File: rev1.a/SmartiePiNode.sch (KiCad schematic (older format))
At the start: 48 parts, among them CN1 USBMICROb, CN2 ST-LINK, CN3 SX1238_TRX_HEADER, SW1 SW_PUSH, U1 ISL91127IR, U2 STM32L052_LQFP48, X1 8MHz(16pF), X2 ABS25-32.768KHZ-6-T

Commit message: footprints
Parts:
- C1, C10, C11, C12, C13, C14, C15, C16, C17, C18, C19, C2, C3, C4, C5, C6, C7, C8, C9: footprint (none) -> Capacitors_SMD:C_0603
- CN1: footprint (none) -> amphenol-microusb-10118194:amphenol-microusb-10118194
- CN2: footprint (none) -> Pin_Headers:Pin_Header_Straight_1x05
- CN3: footprint (none) -> Pin_Headers:Pin_Header_Straight_2x10
- D1: footprint (none) -> digikey-footprints:MicroSD_2908-05WB-MG
- R1, R10, R11, R12, R13, R14, R2, R3, R4, R5, R6, R7, R8, R9: footprint (none) -> Resistors_SMD:R_0603
- SD1: footprint MF_Connectors_MF-MICROSD -> amphenol-microsd-114-00841-68:amphenol-microsd-1140084168
- U1: footprint (none) -> Housings_DFN_QFN:QFN-20-1EP_4x4mm_Pitch0.5mm
- U2: footprint (none) -> Housings_QFP:LQFP-48_7x7mm_Pitch0.5mm

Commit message: hse selection and footprint
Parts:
- removed X2: ABS25-32.768KHZ-6-T, symbol Crystal_Small
- added X?: ABS25-32.768KHZ-6-T, symbol abracon-abs25
- BT1: footprint (none) -> mpd-bh123a:mpd-BH123A
- X1: footprint (none) -> Crystals:Crystal_HC49-SD_SMD
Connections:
- net at C19.2, R14.1: now also X?.1
- net at C18.2, R13.1: now also X?.4
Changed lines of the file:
@@
 LIBS:sw-push
 LIBS:micro-sd-card
+LIBS:crystal_small
 LIBS:SmartiePiNode-cache
 EELAYER 26 0
@@
 F 0 "X1" V 6745 2780 50  0000 L CNN
 F 1 "8MHz(16pF)" V 6960 2595 50  0000 L CNN
-F 2 "" H 6815 2740 50  0001 C CNN
+F 2 "Crystals:Crystal_HC49-SD_SMD" H 6815 2740 50  0001 C CNN
 F 3 "" H 6815 2740 50  0001 C CNN
 	1    6815 2740
@@
 Wire Wire Line
 	10140 2790 9825 2790
-$Comp
-L Crystal_Small X2
-U 1 1 5B098328
-P 10575 2835
-F 0 "X2" V 10510 2870 50  0000 L CNN
-F 1 "ABS25-32.768KHZ-6-T" V 10775 2070 50  0000 L CNN
-F 2 "" H 10575 2835 50  0001 C CNN
-F 3 "" H 10575 2835 50  0001 C CNN
-	1    10575 2835
-	0    1    1    0
-$EndComp
 Wire Wire Line
 	10340 2890 10395 2890
@@
 U 1 1 5B098883
 P 10870 2735
-F 0 "C18" V 10830 2805 50  0000 C CNN
+F 0 "C18" V 10835 2640 50  0000 C CNN
 F 1 "4.3pF" V 10965 2735 50  0000 C CNN
 F 2 "Capacitors_SMD:C_0603" H 10870 2735 50  0001 C CNN
@@
 U 1 1 5B098936
 P 10870 2935
-F 0 "C19" V 10830 3005 50  0000 C CNN
+F 0 "C19" V 10835 2840 50  0000 C CNN
 F 1 "4.3pF" V 10975 2930 50  0000 C CNN
 F 2 "Capacitors_SMD:C_0603" H 10870 2935 50  0001 C CNN
@@
 F 0 "BT1" V 1380 3135 50  0000 L CNN
 F 1 "CR123A" V 1650 3070 50  0000 L CNN
-F 2 "" V 1525 3220 50  0001 C CNN
+F 2 "mpd-bh123a:mpd-BH123A" V 1525 3220 50  0001 C CNN
 F 3 "" V 1525 3220 50  0001 C CNN
 	1    1525 3160
@@
 Text Notes 5500 5950 0    39   ~ 0
 second stage output filter goes here.
+$Comp
+L abracon-abs25 X?
+U 1 1 5B12A6FF
+P 10575 2835
+F 0 "X?" V 10510 2880 50  0000 L CNN
+F 1 "ABS25-32.768KHZ-6-T" V 10765 2080 50  0000 L CNN
+F 2 "" H 10575 2835 50  0001 C CNN
+F 3 "" H 10575 2835 50  0001 C CNN
+	1    10575 2835
+	0    1    1    0
+$EndComp
 $EndSCHEMATC

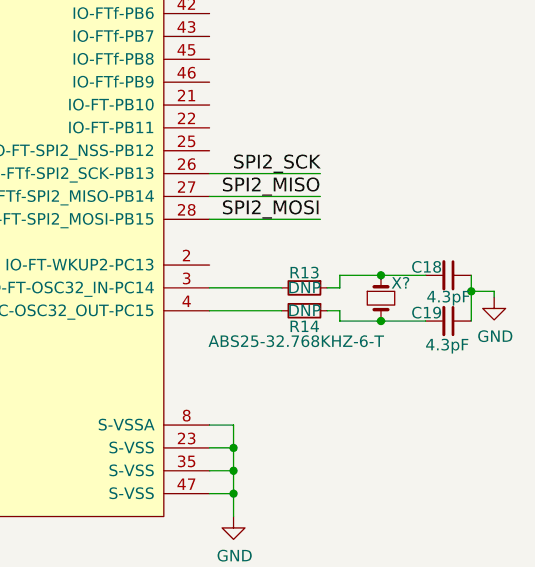
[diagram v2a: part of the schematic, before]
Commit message: L1 part selection, footprint and 3d model creation.
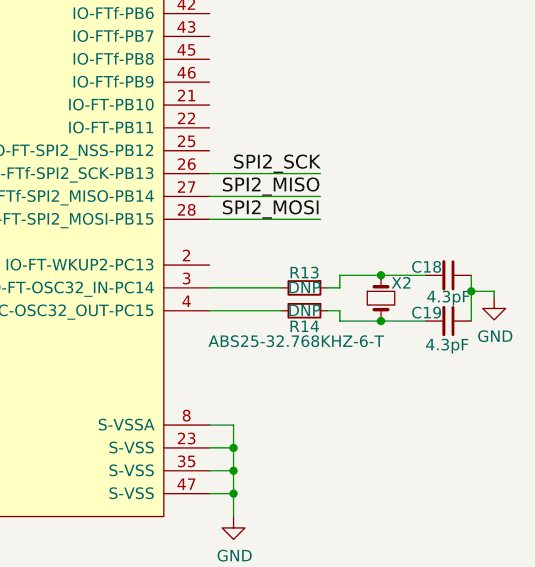
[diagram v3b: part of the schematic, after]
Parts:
- L1: footprint (none) -> murata-1277AS-H-1R0M:murata-1277AS-H-1R0M
- X2: renamed from X?; footprint (none) -> abracon-abs25:abracon-abs25
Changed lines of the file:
@@
 F 0 "L1" V 3565 5480 50  0000 C CNN
 F 1 "1uH" V 3460 5485 50  0000 C CNN
-F 2 "" H 3500 5480 50  0001 C CNN
+F 2 "murata-1277AS-H-1R0M:murata-1277AS-H-1R0M" H 3500 5480 50  0001 C CNN
 F 3 "" H 3500 5480 50  0001 C CNN
 	1    3500 5480
@@
 second stage output filter goes here.
 $Comp
-L abracon-abs25 X?
+L abracon-abs25 X2
 U 1 1 5B12A6FF
 P 10575 2835
-F 0 "X?" V 10510 2880 50  0000 L CNN
+F 0 "X2" V 10510 2880 50  0000 L CNN
 F 1 "ABS25-32.768KHZ-6-T" V 10765 2080 50  0000 L CNN
-F 2 "" H 10575 2835 50  0001 C CNN
+F 2 "abracon-abs25:abracon-abs25" H 10575 2835 50  0001 C CNN
 F 3 "" H 10575 2835 50  0001 C CNN
 	1    10575 2835

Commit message: x1 and x2 footprint and 3d models added to cvpcb
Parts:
- D1: footprint digikey-footprints:MicroSD_2908-05WB-MG -> Diodes_SMD:SOD-123
- D2: footprint (none) -> Diodes_SMD:SOD-123
- F1, L2: footprint (none) -> Capacitors_SMD:C_0603
- SW1: footprint (none) -> te-1825966-1:SWITCH_1825966_1
- X1: footprint Crystals:Crystal_HC49-SD_SMD -> abracon-abm10:abracon-abm10
- X2: footprint abracon-abs25:abracon-abs25 -> abracon-abs07:abracon-abs07
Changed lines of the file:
@@
 F 0 "SW1" H 6055 3085 50  0000 C CNN
 F 1 "SW_PUSH" H 6195 2930 50  0000 C CNN
-F 2 "" H 6180 2990 60  0001 C CNN
+F 2 "te-1825966-1:SWITCH_1825966_1" H 6180 2990 60  0001 C CNN
 F 3 "" H 6180 2990 60  0000 C CNN
 	1    6180 2990
@@
 F 0 "X1" V 6745 2780 50  0000 L CNN
 F 1 "8MHz(16pF)" V 6960 2595 50  0000 L CNN
-F 2 "Crystals:Crystal_HC49-SD_SMD" H 6815 2740 50  0001 C CNN
+F 2 "abracon-abm10:abracon-abm10" H 6815 2740 50  0001 C CNN
 F 3 "" H 6815 2740 50  0001 C CNN
 	1    6815 2740
@@
 F 0 "D2" H 910 6235 50  0000 C CNN
 F 1 "SCHOTTKY" H 860 6080 50  0000 C CNN
-F 2 "" V 910 6150 50  0001 C CNN
+F 2 "Diodes_SMD:SOD-123" V 910 6150 50  0001 C CNN
 F 3 "" V 910 6150 50  0001 C CNN
 	1    910  6150
@@
 F 0 "D1" H 910 6005 50  0000 C CNN
 F 1 "SCHOTTKY" H 840 5850 50  0000 C CNN
-F 2 "digikey-footprints:MicroSD_2908-05WB-MG" V 910 5920 50  0001 C CNN
+F 2 "Diodes_SMD:SOD-123" V 910 5920 50  0001 C CNN
 F 3 "" V 910 5920 50  0001 C CNN
 	1    910  5920
@@
 F 0 "L2" V 7775 5330 50  0000 C CNN
 F 1 "ferrite" V 7875 5330 50  0000 C CNN
-F 2 "" H 7825 5330 50  0001 C CNN
+F 2 "Capacitors_SMD:C_0603" H 7825 5330 50  0001 C CNN
 F 3 "" H 7825 5330 50  0001 C CNN
 	1    7825 5330
@@
 F 0 "F1" H 1380 6095 50  0000 C CNN
 F 1 "500mA" H 1380 6205 50  0000 C CNN
-F 2 "" H 1380 6150 50  0001 C CNN
+F 2 "Capacitors_SMD:C_0603" H 1380 6150 50  0001 C CNN
 F 3 "" H 1380 6150 50  0001 C CNN
 	1    1380 6150
@@
 F 0 "X2" V 10510 2880 50  0000 L CNN
 F 1 "ABS25-32.768KHZ-6-T" V 10765 2080 50  0000 L CNN
-F 2 "abracon-abs25:abracon-abs25" H 10575 2835 50  0001 C CNN
+F 2 "abracon-abs07:abracon-abs07" H 10575 2835 50  0001 C CNN
 F 3 "" H 10575 2835 50  0001 C CNN
 	1    10575 2835

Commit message: stm32l052 footprint and 3d model added
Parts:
- F1: footprint Capacitors_SMD:C_0603 -> belfuse-c2q:belfuse-c2q
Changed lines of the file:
@@
 F 0 "F1" H 1380 6095 50  0000 C CNN
 F 1 "500mA" H 1380 6205 50  0000 C CNN
-F 2 "Capacitors_SMD:C_0603" H 1380 6150 50  0001 C CNN
+F 2 "belfuse-c2q:belfuse-c2q" H 1380 6150 50  0001 C CNN
 F 3 "" H 1380 6150 50  0001 C CNN
 	1    1380 6150

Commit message: stm32l052 cvpcb
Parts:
- U2: footprint Housings_QFP:LQFP-48_7x7mm_Pitch0.5mm -> st-stm32l052-lqfp48:STM32L052C8T6
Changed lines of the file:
@@
 F 0 "U2" H 7620 -460 60  0000 C CNN
 F 1 "STM32L052_LQFP48" H 8615 2530 60  0000 C CNN
-F 2 "Housings_QFP:LQFP-48_7x7mm_Pitch0.5mm" H 7875 1690 60  0001 C CNN
+F 2 "st-stm32l052-lqfp48:STM32L052C8T6" H 7875 1690 60  0001 C CNN
 F 3 "" H 7875 1690 60  0001 C CNN
 	1    7875 1690

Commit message: double check and fix footprints
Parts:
- C1: footprint Capacitors_SMD:C_0603 -> Capacitors_SMD:C_0805
- D1, D2: footprint Diodes_SMD:SOD-123 -> onsemi-NRVB120VLSFT1G:onsemi-NRVB120VLSFT1G
- L2: footprint Capacitors_SMD:C_0603 -> bourns-MH1608-601Y:MH1608-601Y
- U1: footprint Housings_DFN_QFN:QFN-20-1EP_4x4mm_Pitch0.5mm -> intersil-isl91127ir:intersil-isl91127ir
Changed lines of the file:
@@
 F 0 "U1" H 3065 5695 60  0000 C CNN
 F 1 "ISL91127IR" H 3520 7105 60  0000 C CNN
-F 2 "Housings_DFN_QFN:QFN-20-1EP_4x4mm_Pitch0.5mm" H 3520 6400 60  0001 C CNN
+F 2 "intersil-isl91127ir:intersil-isl91127ir" H 3520 6400 60  0001 C CNN
 F 3 "" H 3520 6400 60  0001 C CNN
 	1    3520 6400
@@
 F 0 "C1" H 1790 6370 50  0000 L CNN
 F 1 "DNP" H 1790 6240 50  0000 L CNN
-F 2 "Capacitors_SMD:C_0603" H 1785 6305 50  0001 C CNN
+F 2 "Capacitors_SMD:C_0805" H 1785 6305 50  0001 C CNN
 F 3 "" H 1785 6305 50  0001 C CNN
 	1    1785 6305
@@
 F 0 "D2" H 910 6235 50  0000 C CNN
 F 1 "SCHOTTKY" H 860 6080 50  0000 C CNN
-F 2 "Diodes_SMD:SOD-123" V 910 6150 50  0001 C CNN
+F 2 "onsemi-NRVB120VLSFT1G:onsemi-NRVB120VLSFT1G" V 910 6150 50  0001 C CNN
 F 3 "" V 910 6150 50  0001 C CNN
 	1    910  6150
@@
 F 0 "D1" H 910 6005 50  0000 C CNN
 F 1 "SCHOTTKY" H 840 5850 50  0000 C CNN
-F 2 "Diodes_SMD:SOD-123" V 910 5920 50  0001 C CNN
+F 2 "onsemi-NRVB120VLSFT1G:onsemi-NRVB120VLSFT1G" V 910 5920 50  0001 C CNN
 F 3 "" V 910 5920 50  0001 C CNN
 	1    910  5920
@@
 F 0 "L2" V 7775 5330 50  0000 C CNN
 F 1 "ferrite" V 7875 5330 50  0000 C CNN
-F 2 "Capacitors_SMD:C_0603" H 7825 5330 50  0001 C CNN
+F 2 "bourns-MH1608-601Y:MH1608-601Y" H 7825 5330 50  0001 C CNN
 F 3 "" H 7825 5330 50  0001 C CNN
 	1    7825 5330

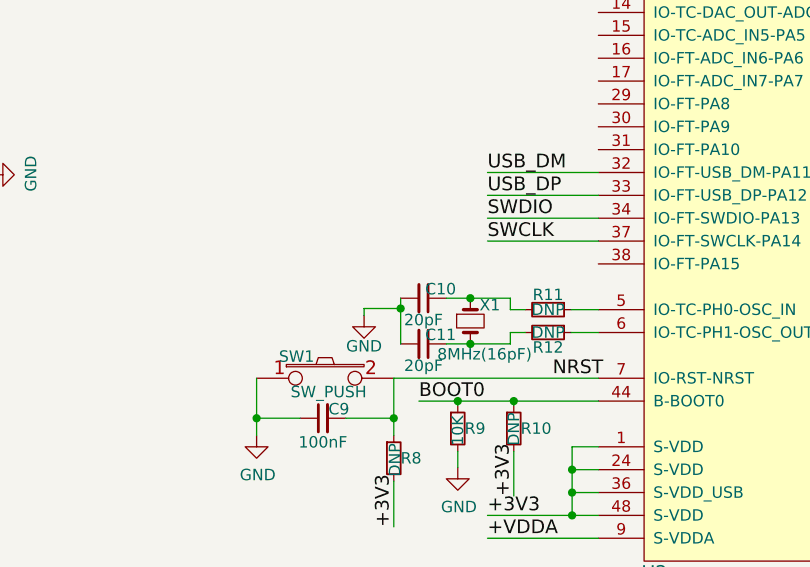
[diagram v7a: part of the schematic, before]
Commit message: new abm10 schematic symbol and circuitry
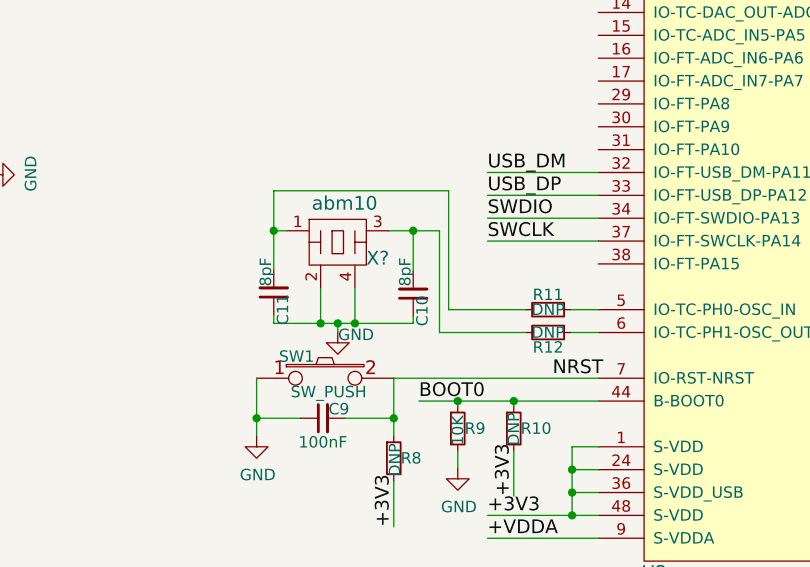
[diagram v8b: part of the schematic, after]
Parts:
- removed X1: 8MHz(16pF), abracon-abm10:abracon-abm10, symbol Crystal_Small
- added X?: abm10, symbol abracon-abm10
- C10, C11: value 20pF -> 8pF
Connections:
- net GND: now also C10.1, C11.1, X?.2, X?.4; no longer C10.2, C11.2
- net at R11.2: now also C11.2, X?.1; no longer C10.1
- net at R12.2: now also C10.2, X?.3; no longer C11.1
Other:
- moved on the sheet: C10, C11
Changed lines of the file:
@@
 LIBS:micro-sd-card
 LIBS:crystal_small
+LIBS:abracon-abm10
 LIBS:SmartiePiNode-cache
 EELAYER 26 0
@@
 USB_DP
 $Comp
-L Crystal_Small X1
-U 1 1 5B0960C7
-P 6815 2740
-F 0 "X1" V 6745 2780 50  0000 L CNN
-F 1 "8MHz(16pF)" V 6960 2595 50  0000 L CNN
-F 2 "abracon-abm10:abracon-abm10" H 6815 2740 50  0001 C CNN
-F 3 "" H 6815 2740 50  0001 C CNN
-	1    6815 2740
-	0    1    1    0
-$EndComp
-$Comp
 L R_Small R11
 U 1 1 5B09626D
@@
 $EndComp
 $Comp
-L C_Small C10
-U 1 1 5B096D6A
-P 6610 2640
-F 0 "C10" V 6570 2715 50  0000 C CNN
-F 1 "20pF" V 6705 2640 50  0000 C CNN
-F 2 "Capacitors_SMD:C_0603" H 6610 2640 50  0001 C CNN
-F 3 "" H 6610 2640 50  0001 C CNN
-	1    6610 2640
-	0    1    1    0
-$EndComp
-$Comp
 L C_Small C11
 U 1 1 5B096F75
-P 6610 2840
-F 0 "C11" V 6570 2915 50  0000 C CNN
-F 1 "20pF" V 6705 2840 50  0000 C CNN
-F 2 "Capacitors_SMD:C_0603" H 6610 2840 50  0001 C CNN
-F 3 "" H 6610 2840 50  0001 C CNN
-	1    6610 2840
-	0    1    1    0
-$EndComp
-Wire Wire Line
-	6710 2640 6990 2640
-Wire Wire Line
-	6990 2640 6990 2690
-Wire Wire Line
-	6990 2690 7055 2690
-Connection ~ 6815 2840
-Wire Wire Line
-	6990 2840 6710 2840
-Wire Wire Line
-	6990 2790 6990 2840
-Wire Wire Line
-	7055 2790 6990 2790
+P 5955 2615
+F 0 "C11" V 5915 2690 50  0000 C CNN
+F 1 "8pF" V 5990 2525 50  0000 C CNN
+F 2 "Capacitors_SMD:C_0603" H 5955 2615 50  0001 C CNN
+F 3 "" H 5955 2615 50  0001 C CNN
+	1    5955 2615
+	-1   0    0    1
+$EndComp
+Wire Wire Line
+	6720 2690 7055 2690
+Wire Wire Line
+	6680 2790 7055 2790
 Wire Wire Line
 	7375 2790 7255 2790
@@
 Wire Wire Line
 	2820 5950 2770 5950
-Connection ~ 6815 2640
-$Comp
-L GND #PWR014
-U 1 1 5B097780
-P 6350 2715
-F 0 "#PWR014" H 6350 2465 50  0001 C CNN
-F 1 "GND" H 6350 2580 50  0000 C CNN
-F 2 "" H 6350 2715 50  0001 C CNN
-F 3 "" H 6350 2715 50  0001 C CNN
-	1    6350 2715
-	1    0    0    -1
-$EndComp
-Wire Wire Line
-	6350 2715 6350 2685
-Wire Wire Line
-	6350 2685 6510 2685
-Wire Wire Line
-	6510 2640 6510 2840
-Connection ~ 6510 2685
 $Comp
 L R_Small R14
@@
 	0    1    1    0
 $EndComp
+$Comp
+L abracon-abm10 X?
+U 1 1 5B1A86B5
+P 6260 2395
+F 0 "X?" H 6410 2325 60  0000 C CNN
+F 1 "abm10" H 6265 2565 60  0000 C CNN
+F 2 "" H 6260 2395 60  0001 C CNN
+F 3 "" H 6260 2395 60  0001 C CNN
+	1    6260 2395
+	1    0    0    -1
+$EndComp
+$Comp
+L C_Small C10
+U 1 1 5B096D6A
+P 6565 2620
+F 0 "C10" V 6525 2695 50  0000 C CNN
+F 1 "8pF" V 6600 2525 50  0000 C CNN
+F 2 "Capacitors_SMD:C_0603" H 6565 2620 50  0001 C CNN
+F 3 "" H 6565 2620 50  0001 C CNN
+	1    6565 2620
+	-1   0    0    1
+$EndComp
+Wire Wire Line
+	6720 2170 6720 2690
+Wire Wire Line
+	5955 2170 6720 2170
+Wire Wire Line
+	5955 2345 6010 2345
+Wire Wire Line
+	6460 2345 6680 2345
+Wire Wire Line
+	6680 2345 6680 2790
+Wire Wire Line
+	6565 2520 6565 2345
+Connection ~ 6565 2345
+Wire Wire Line
+	5955 2170 5955 2515
+Connection ~ 5955 2345
+Wire Wire Line
+	5955 2715 5955 2750
+Wire Wire Line
+	5955 2750 6565 2750
+Wire Wire Line
+	6565 2750 6565 2720
+Wire Wire Line
+	6160 2595 6160 2750
+Connection ~ 6160 2750
+Wire Wire Line
+	6310 2595 6310 2750
+Connection ~ 6310 2750
+Wire Wire Line
+	6235 2750 6235 2785
+Connection ~ 6235 2750
+$Comp
+L GND #PWR?
+U 1 1 5B1AE42D
+P 6235 2785
+F 0 "#PWR?" H 6235 2535 50  0001 C CNN
+F 1 "GND" H 6315 2770 50  0000 C CNN
+F 2 "" H 6235 2785 50  0001 C CNN
+F 3 "" H 6235 2785 50  0001 C CNN
+	1    6235 2785
+	1    0    0    -1
+$EndComp
 $EndSCHEMATC
